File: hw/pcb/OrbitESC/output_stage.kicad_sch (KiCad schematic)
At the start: 0 parts

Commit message: Start designing power stage
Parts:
- added C1, C4, C7: 100nF, Capacitor_SMD:C_0402_1005Metric, symbol Device:C
- added C2, C5, C8: 1nF, Capacitor_SMD:C_0603_1608Metric, symbol Device:C
- added C3, C6, C9: 2.2uF, Capacitor_SMD:C_0805_2012Metric, symbol Device:C
- added J3: TermA, TestPoint:TestPoint_Pad_4.0x4.0mm, symbol Connector:Conn_01x01_Female
- added J4: TermB, TestPoint:TestPoint_Pad_4.0x4.0mm, symbol Connector:Conn_01x01_Female
- added J5: TermC, TestPoint:TestPoint_Pad_4.0x4.0mm, symbol Connector:Conn_01x01_Female
- added Q1, Q2, Q3, Q4, Q5, Q6: MCAC80N10Y, Project Mosfets:TRANS_BSC076N06NS3-G, symbol Project Mosfets:MCAC80N10Y
- added R1, R13, R7: 4.99k, Resistor_SMD:R_0603_1608Metric, symbol Device:R_US
- added R10, R14, R16, R2, R4, R8: 10, symbol Device:R_US
- added R11, R17, R5: 39k, symbol Device:R_US
- added R12, R18, R6: 0.01, Resistor_SMD:R_2512_6332Metric, symbol Device:R_US
- added R15, R3, R9: 30k, Resistor_SMD:R_0603_1608Metric, symbol Device:R_US
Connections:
- new net: Q2.2 (G), R4.2, R5.1
- new net: Q4.2 (G), R10.2, R11.1
- new net: Q3.2 (G), R8.2
- new net: Q1.2 (G), R2.2
- new net: Q5.2 (G), R14.2
- new net: Q6.2 (G), R16.2, R17.1
- new net A_ISENSE_P: C2.1, Q2.3 (S), R5.2, R6.1
- new net B_ISENSE_P: C5.1, Q4.3 (S), R11.2, R12.1
- new net C_ISENSE_P: C8.1, Q6.3 (S), R17.2, R18.1
- new net GDH_A: R2.1
- new net GDH_B: R8.1
- new net GDH_C: R14.1
- new net GDL_A: R4.1
- new net GDL_B: R10.1
- new net GDL_C: R16.1
- new net GND: C1.2, C2.2, C3.2, C4.2, C5.2, C6.2, C7.2, C8.2, C9.2, R1.1, R12.2, R13.1, R18.2, R6.2, R7.1
- new net SH_A: J3.1 (Pin_1), Q1.3 (S), Q2.1 (D), R3.2
- new net SH_B: J4.1 (Pin_1), Q3.3 (S), Q4.1 (D), R9.2
- new net SH_C: J5.1 (Pin_1), Q5.3 (S), Q6.1 (D), R15.2
- new net VA_FB: C1.1, C4.1, R1.2, R3.1, R7.2, R9.1
- new net VA_FC: C7.1, R13.2, R15.1
- new net VDC: C3.1, C6.1, C9.1, Q1.1 (D), Q3.1 (D), Q5.1 (D)

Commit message: Add power stage components
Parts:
- added C10, C11: 1uF, Capacitor_SMD:C_0402_1005Metric, symbol Device:C
- added R19: 1k, Resistor_SMD:R_0402_1005Metric, symbol Device:R_US
- added R20: 10k, Resistor_SMD:R_0402_1005Metric, symbol Device:R_US
- added TH1, TH2: 10k NTC, Resistor_SMD:R_0402_1005Metric, symbol Device:Thermistor_NTC_US
- R1, R13: value 4.99k -> 1k; footprint Resistor_SMD:R_0603_1608Metric -> Resistor_SMD:R_0402_1005Metric; JLCPCB C23046 -> C11702
- R10, R11, R14, R16, R17, R2, R4, R5, R8: footprint (none) -> Resistor_SMD:R_0402_1005Metric
- R15, R3, R9: value 30k -> 10k; footprint Resistor_SMD:R_0603_1608Metric -> Resistor_SMD:R_0402_1005Metric; JLCPCB C22984 -> C25744
- R7: value 4.99k -> 10k; footprint Resistor_SMD:R_0603_1608Metric -> Resistor_SMD:R_0402_1005Metric; JLCPCB C23046 -> C25744
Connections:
- net GND: now also R19.1; no longer R7.1
- net SH_B: now also R15.2; no longer R9.2
- net SH_C: now also R20.2; no longer R15.2
- net VA_FB: no longer C4.1, R7.2, R9.1
- net VA_FC renamed VB_FB
- net VB_FB: now also C4.1; no longer C7.1
- new net +3.3V: TH1.1, TH2.1
- new net GNDD: C10.2, C11.2, R7.2, R9.2
- new net TempA: C10.1, R7.1, TH1.2
- new net TempB: C11.1, R9.1, TH2.2
- new net VC_FB: C7.1, R19.2, R20.1
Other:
- note added: "Temp Sense Bottom"
- note added: "Temp Sense Top"

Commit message: Schematic checklist runthrough
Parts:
- J3, J4, J5: DigiKey (none) -> N/A
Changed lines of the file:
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@@
+      (effects (font (size 1.27 1.27)) hide)
+    )
+    (property "DigiKey" "N/A" (id 4) (at 172.72 83.82 0)
       (effects (font (size 1.27 1.27)) hide)
     )
@@
       (effects (font (size 1.27 1.27)) hide)
     )
+    (property "DigiKey" "N/A" (id 4) (at 260.35 83.82 0)
+      (effects (font (size 1.27 1.27)) hide)
+    )
     (pin "1")
   )
@@
       (effects (font (size 1.27 1.27)) hide)
     )
+    (property "DigiKey" "N/A" (id 4) (at 85.09 83.82 0)
+      (effects (font (size 1.27 1.27)) hide)
+    )

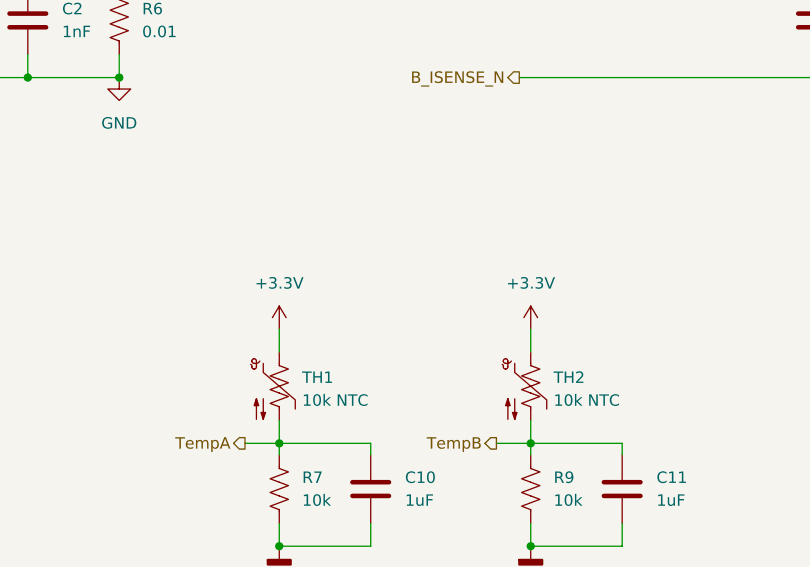
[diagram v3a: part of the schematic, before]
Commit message: Route analogs and power stage sections
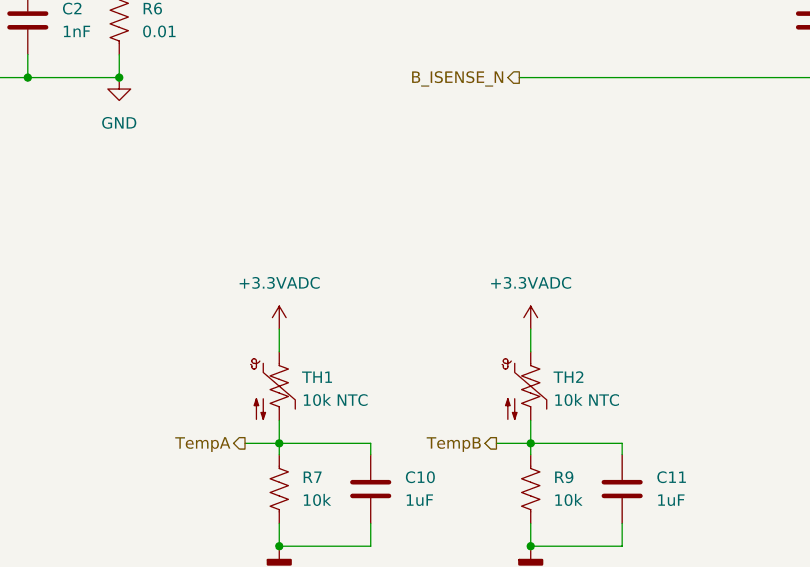
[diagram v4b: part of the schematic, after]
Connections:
- net +3.3V renamed +3.3VADC
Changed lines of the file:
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@@
     (pin "2")
-  )
-  (symbol (lib_id "power:+3.3V") (at 125.73 148.59 0) (unit 1)
-    (in_bom yes) (on_board yes) (fields_autoplaced)
-    (property "Reference" "#PWR015" (id 0) (at 125.73 152.4 0)
-      (effects (font (size 1.27 1.27)) hide)
-    )
-    (property "Value" "+3.3V" (id 1) (at 125.73 143.51 0))
-    (property "Footprint" "" (id 2) (at 125.73 148.59 0)
-      (effects (font (size 1.27 1.27)) hide)
-    )
-    (property "Datasheet" "" (id 3) (at 125.73 148.59 0)
-      (effects (font (size 1.27 1.27)) hide)
-    )
-    (pin "1")
   )
   (symbol (lib_id "Project Mosfets:MCAC80N10Y") (at 252.73 71.12 0) (unit 1)
@@
     (pin "1")
     (pin "2")
+  )
+  (symbol (lib_id "power:+3.3VADC") (at 97.79 148.59 0) (unit 1)
+    (in_bom yes) (on_board yes) (fields_autoplaced)
+    (property "Reference" "#PWR0141" (id 0) (at 101.6 149.86 0)
+      (effects (font (size 1.27 1.27)) hide)
+    )
+    (property "Value" "+3.3VADC" (id 1) (at 97.79 143.51 0))
+    (property "Footprint" "" (id 2) (at 97.79 148.59 0)
+      (effects (font (size 1.27 1.27)) hide)
+    )
+    (property "Datasheet" "" (id 3) (at 97.79 148.59 0)
+      (effects (font (size 1.27 1.27)) hide)
+    )
+    (pin "1")
   )
   (symbol (lib_id "Device:R_US") (at 238.76 83.82 90) (unit 1)
@@
     (pin "1")
   )
+  (symbol (lib_id "power:+3.3VADC") (at 125.73 148.59 0) (unit 1)
+    (in_bom yes) (on_board yes) (fields_autoplaced)
+    (property "Reference" "#PWR0142" (id 0) (at 129.54 149.86 0)
+      (effects (font (size 1.27 1.27)) hide)
+    )
+    (property "Value" "+3.3VADC" (id 1) (at 125.73 143.51 0))
+    (property "Footprint" "" (id 2) (at 125.73 148.59 0)
+      (effects (font (size 1.27 1.27)) hide)
+    )
+    (property "Datasheet" "" (id 3) (at 125.73 148.59 0)
+      (effects (font (size 1.27 1.27)) hide)
+    )
+    (pin "1")
+  )
   (symbol (lib_id "Connector:Conn_01x01_Female") (at 85.09 83.82 0) (unit 1)
     (in_bom yes) (on_board yes) (fields_autoplaced)
@@
     (pin "2")
   )
-  (symbol (lib_id "power:+3.3V") (at 97.79 148.59 0) (unit 1)
-    (in_bom yes) (on_board yes) (fields_autoplaced)
-    (property "Reference" "#PWR013" (id 0) (at 97.79 152.4 0)
-      (effects (font (size 1.27 1.27)) hide)
-    )
-    (property "Value" "+3.3V" (id 1) (at 97.79 143.51 0))
-    (property "Footprint" "" (id 2) (at 97.79 148.59 0)
-      (effects (font (size 1.27 1.27)) hide)
-    )
-    (property "Datasheet" "" (id 3) (at 97.79 148.59 0)
-      (effects (font (size 1.27 1.27)) hide)
-    )
-    (pin "1")
-  )
 )

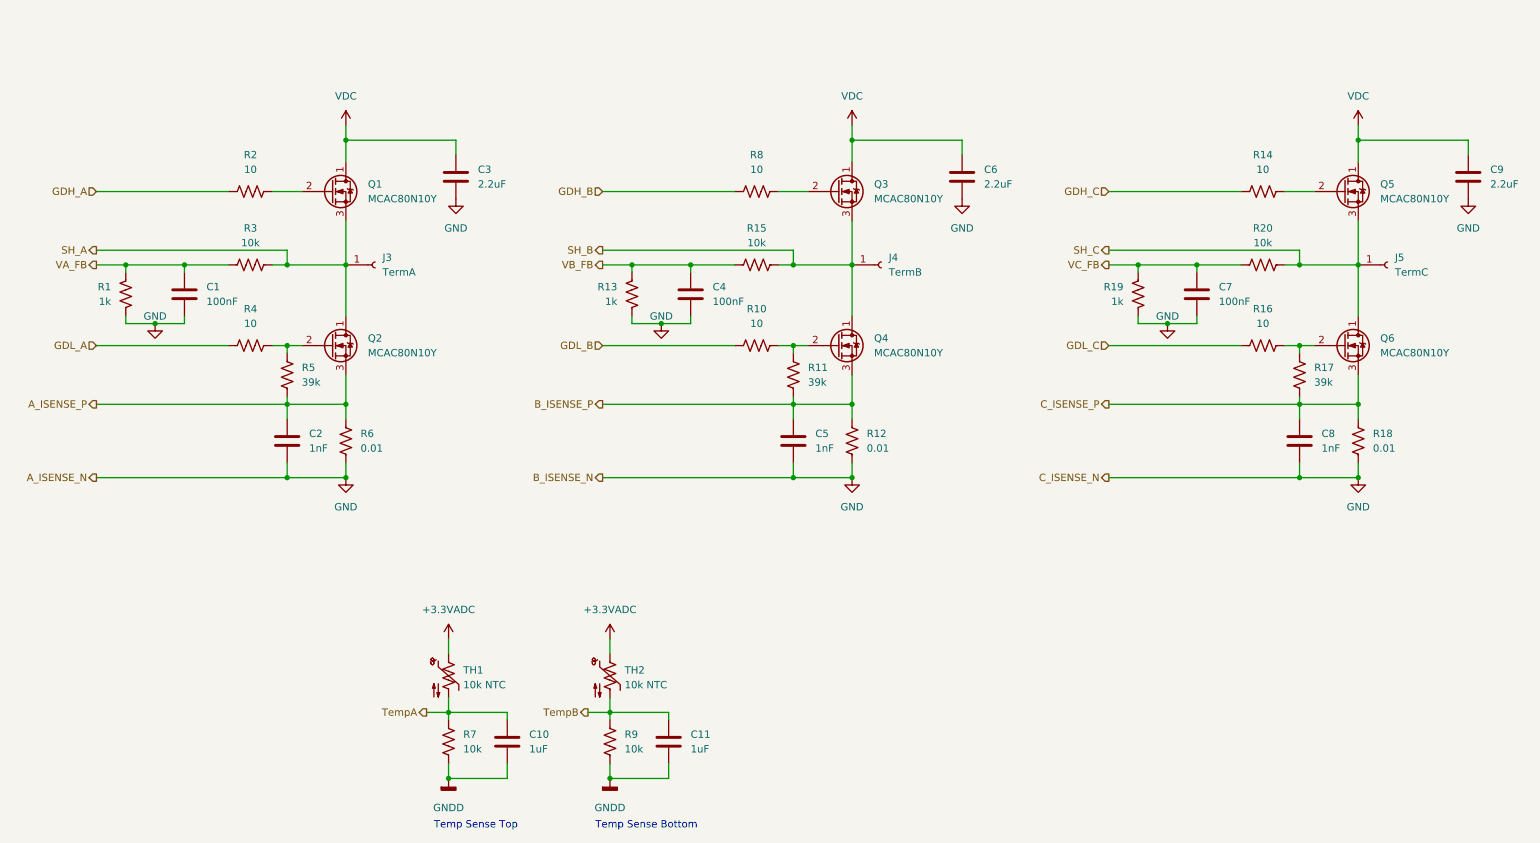
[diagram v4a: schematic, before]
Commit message: Start rework of processor selection after realizing I can't afford manufacturing...
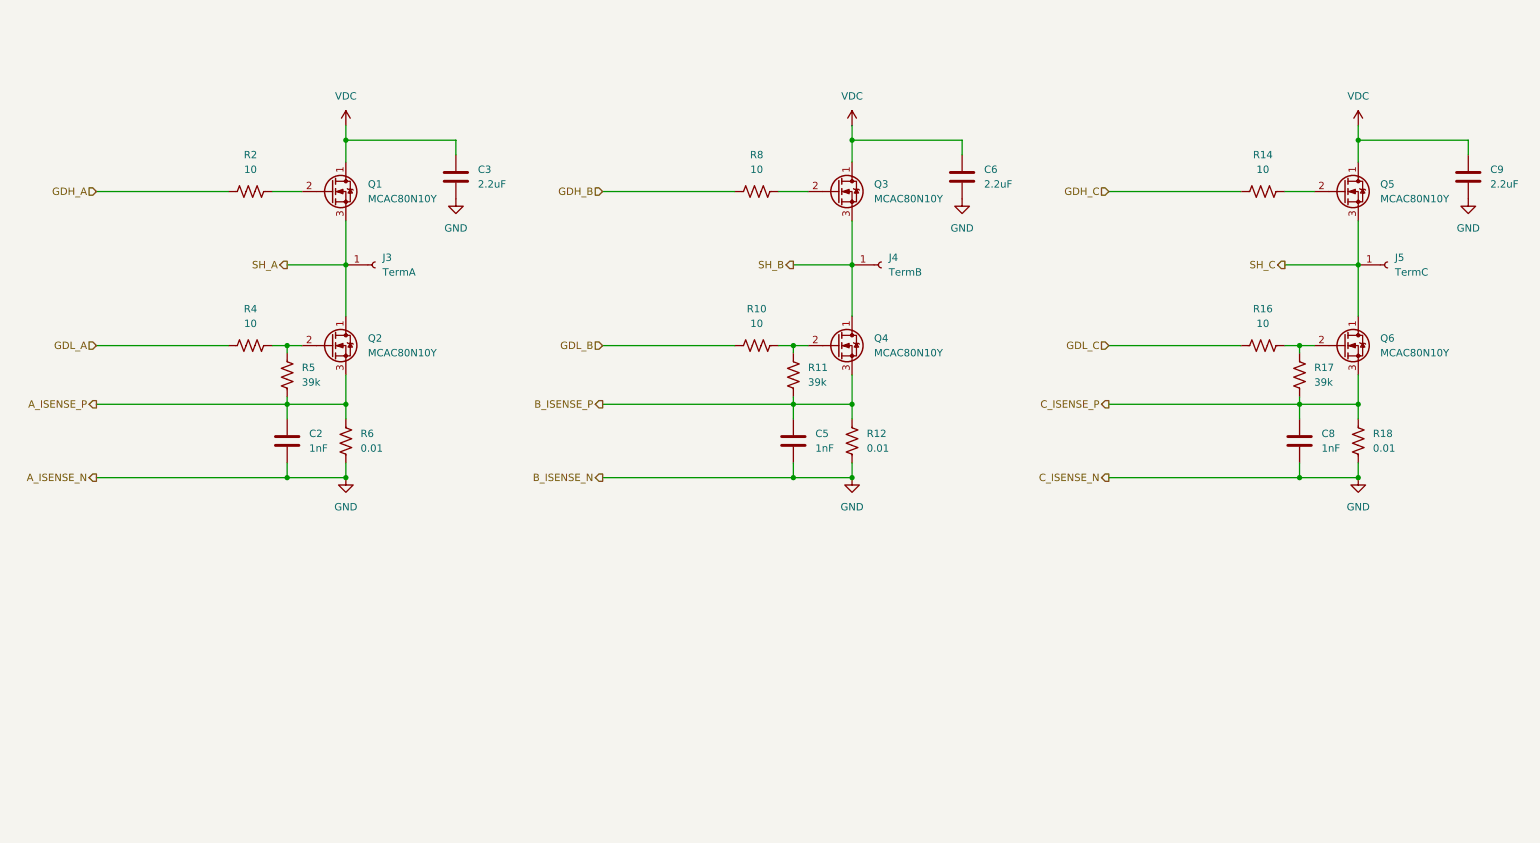
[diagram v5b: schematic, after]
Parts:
- removed C1, C4, C7: 100nF, Capacitor_SMD:C_0402_1005Metric, symbol Device:C
- removed C10, C11: 1uF, Capacitor_SMD:C_0402_1005Metric, symbol Device:C
- removed R1, R13, R19: 1k, Resistor_SMD:R_0402_1005Metric, symbol Device:R_US
- removed R15, R20, R3, R7, R9: 10k, Resistor_SMD:R_0402_1005Metric, symbol Device:R_US
- removed TH1, TH2: 10k NTC, Resistor_SMD:R_0402_1005Metric, symbol Device:Thermistor_NTC_US
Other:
- note removed: "Temp Sense Bottom"
- note removed: "Temp Sense Top"

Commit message: Squash feature/sync_current_ctrl/r0
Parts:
- removed R11, R17, R5: 39k, Resistor_SMD:R_0402_1005Metric, symbol Device:R_US
- added C37: 2.2uF, Capacitor_SMD:C_0805_2012Metric, symbol Device:C
- C2, C5, C8: footprint Capacitor_SMD:C_0603_1608Metric -> Capacitor_SMD:C_0402_1005Metric; JLCPCB C1588 -> (none); LCSC (none) -> C1523
- C3, C6, C9: JLCPCB C49217 -> (none); LCSC (none) -> C49217
- Q1, Q2, Q3, Q4, Q5, Q6: value MCAC80N10Y -> MCAC100N08YA-TP; DigiKey 353-MCAC80N10Y-TPCT-ND -> 353-MCAC100N08YA-TPCT-ND
- R10, R14, R16, R2, R4, R8: value 10 -> 1; JLCPCB C25077 -> (none); LCSC (none) -> C25086
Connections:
- net GND: now also C37.2
- net VDC: now also C37.1
